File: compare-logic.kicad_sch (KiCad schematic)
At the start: 0 parts

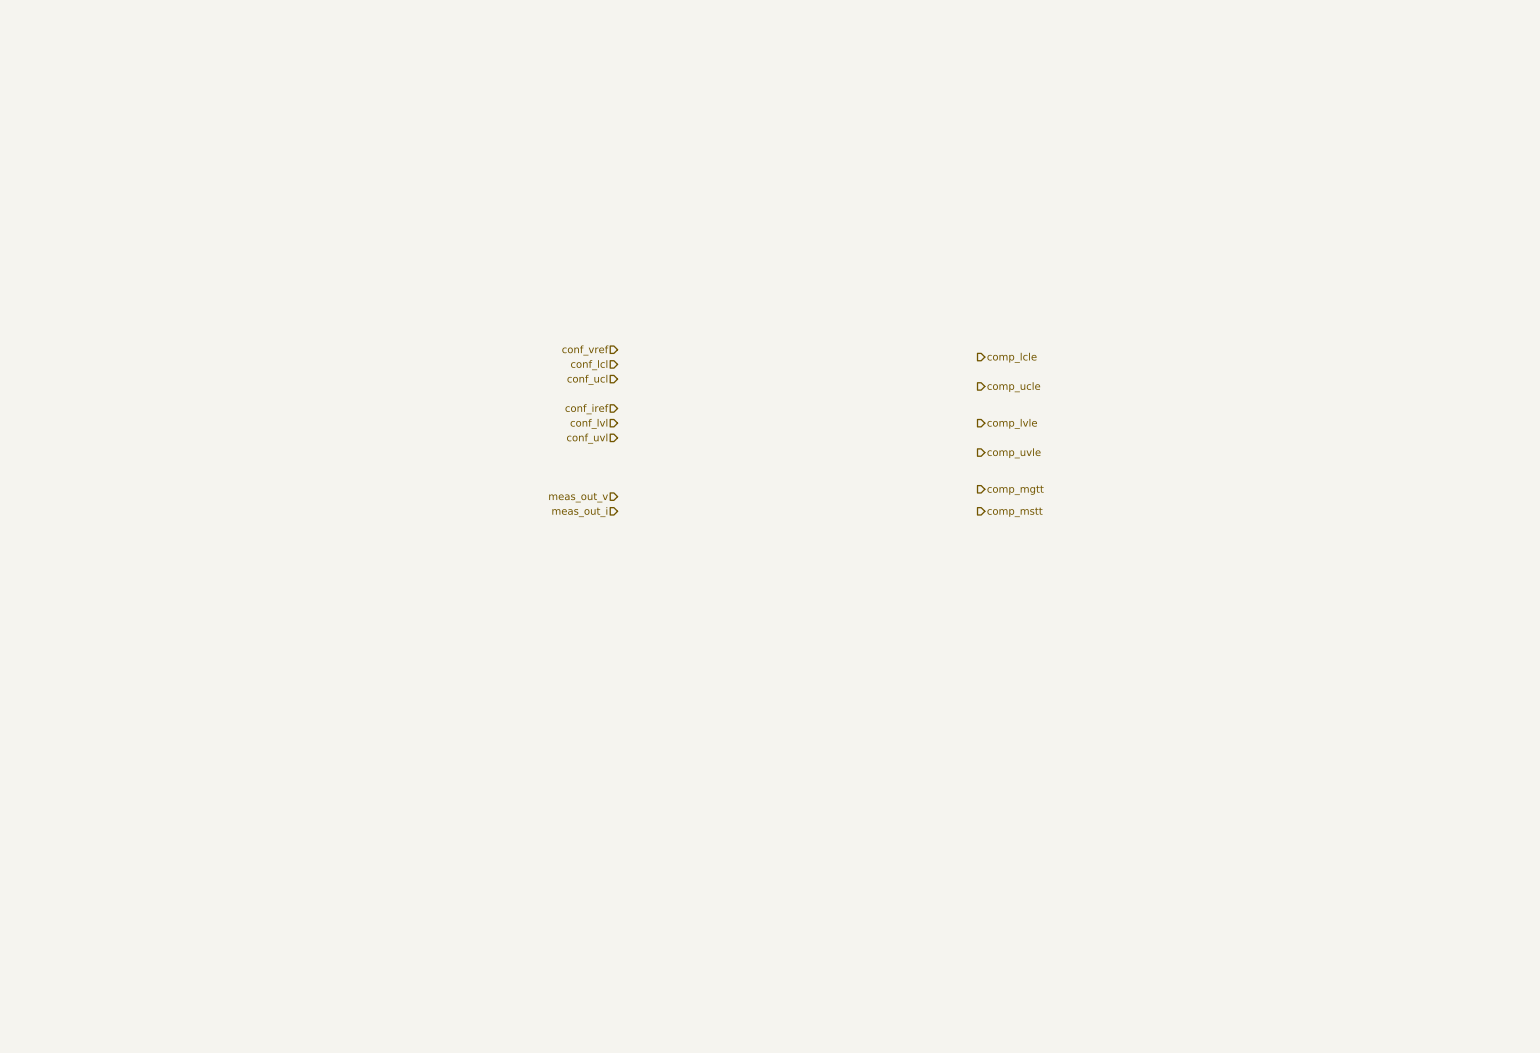
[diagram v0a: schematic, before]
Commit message: add limit-logic comparator opamp tlv9352
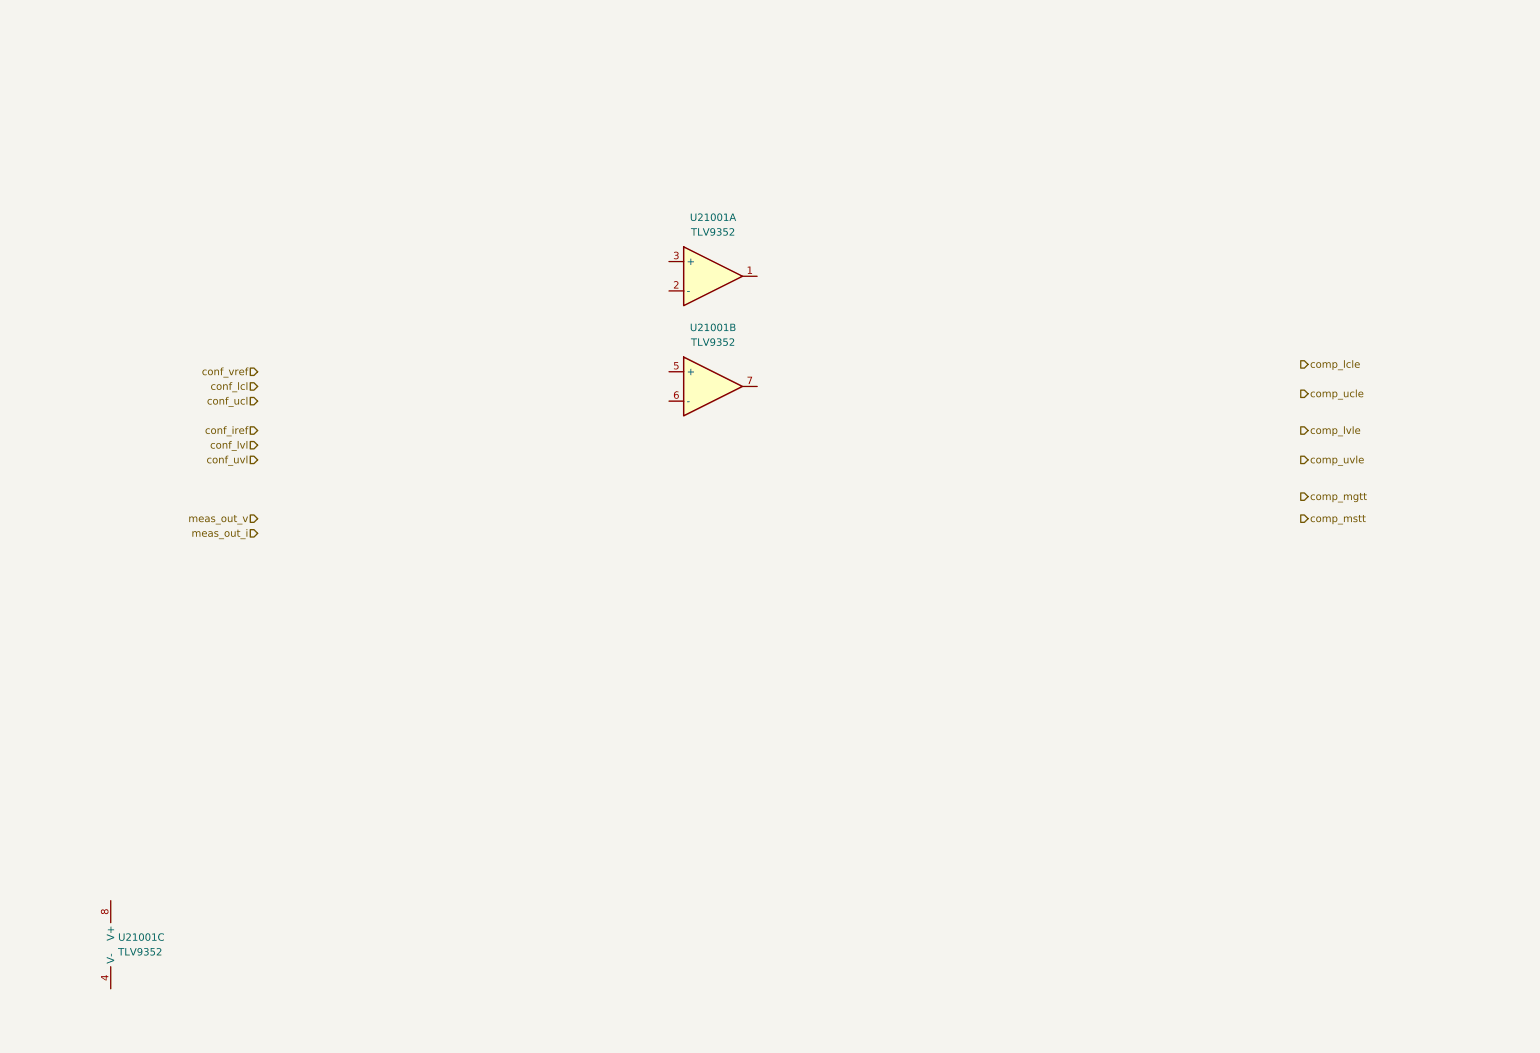
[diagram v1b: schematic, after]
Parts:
- added U21001: TLV9352, Package_SO:SOIC-8_3.9x4.9mm_P1.27mm, symbol pss:Opamp_Dual

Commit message: add compare-logic windows comparator
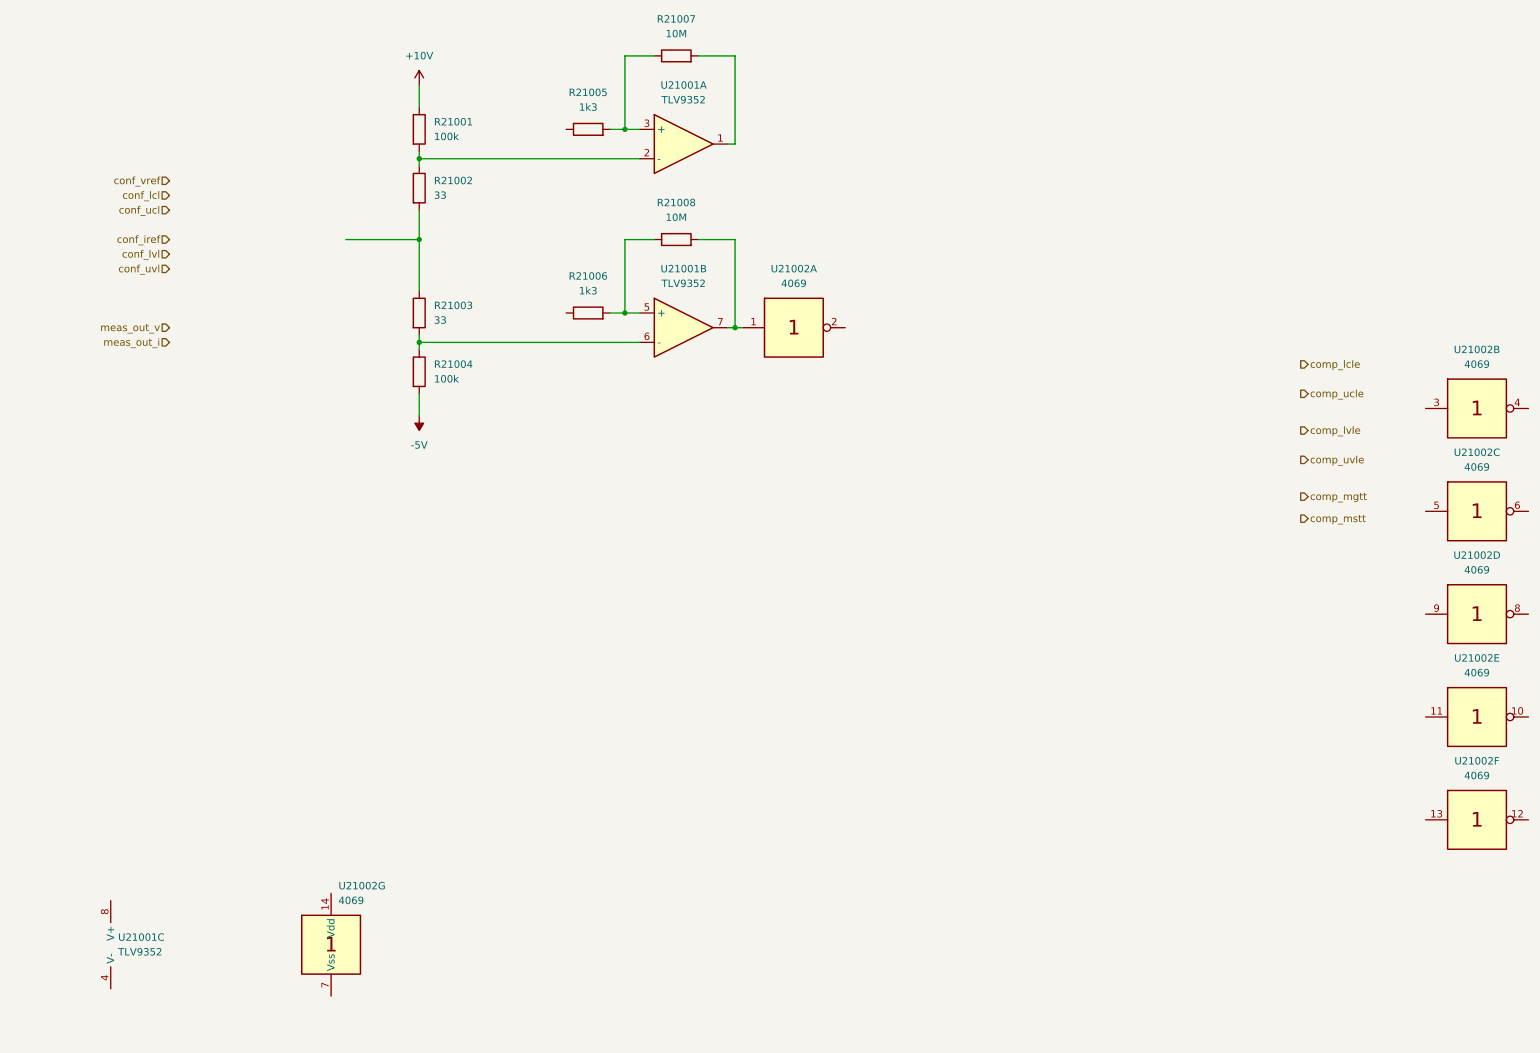
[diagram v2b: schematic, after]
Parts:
- added R21001, R21004: 100k, Resistor_SMD:R_1210_3225Metric_Pad1.30x2.65mm_HandSolder, symbol pss:R
- added R21002, R21003: 33, Resistor_SMD:R_1210_3225Metric_Pad1.30x2.65mm_HandSolder, symbol pss:R
- added R21005, R21006: 1k3, Resistor_SMD:R_1210_3225Metric_Pad1.30x2.65mm_HandSolder, symbol pss:R
- added R21007, R21008: 10M, Resistor_SMD:R_1210_3225Metric_Pad1.30x2.65mm_HandSolder, symbol pss:R
- added U21002: 4069, Package_SO:SOIC-14_3.9x8.7mm_P1.27mm, symbol pss:4069
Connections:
- net at U21001.5 (+): now also R21006.2, R21008.1
- net at U21001.6 (-): now also R21003.2, R21004.1
- net at U21001.7: now also R21008.2, U21002.1
- net at U21001.1: now also R21007.2
- net at U21001.2 (-): now also R21001.2, R21002.1
- net at U21001.3 (+): now also R21005.2, R21007.1
- new net: R21002.2, R21003.1
- new net +10V: R21001.1
- new net -5V: R21004.2
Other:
- moved on the sheet: U21001A, U21001B

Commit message: add window-comparator hirarchical sheet
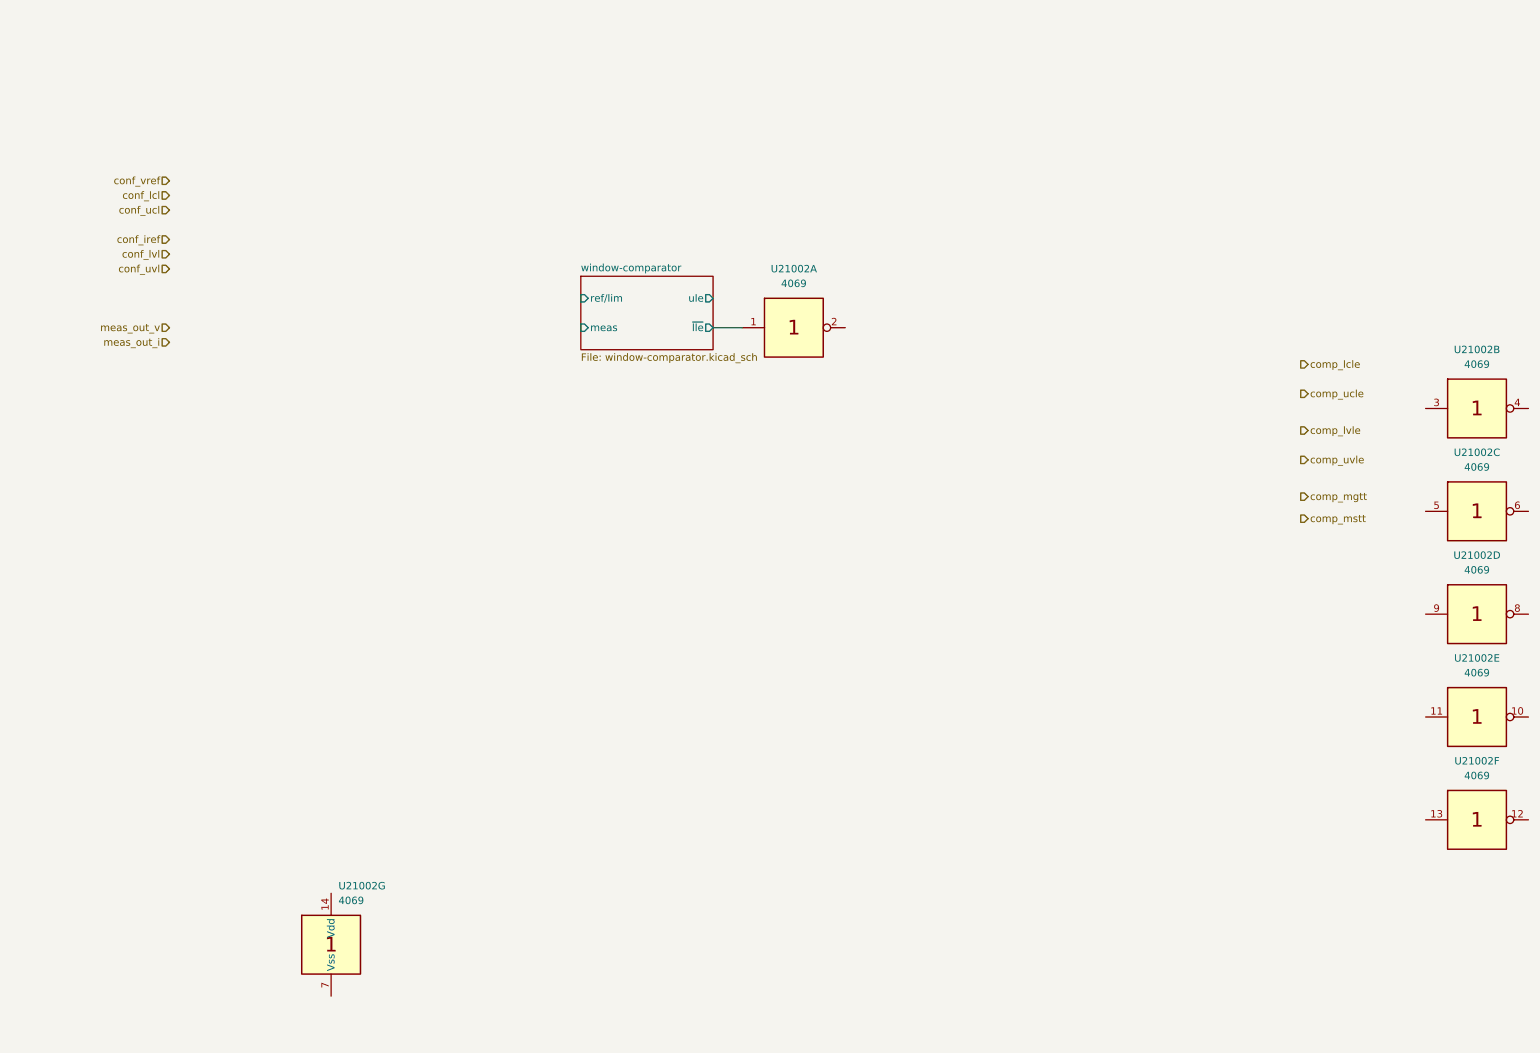
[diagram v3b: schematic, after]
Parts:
- removed R21001, R21004: 100k, Resistor_SMD:R_1210_3225Metric_Pad1.30x2.65mm_HandSolder, symbol pss:R
- removed R21002, R21003: 33, Resistor_SMD:R_1210_3225Metric_Pad1.30x2.65mm_HandSolder, symbol pss:R
- removed R21005, R21006: 1k3, Resistor_SMD:R_1210_3225Metric_Pad1.30x2.65mm_HandSolder, symbol pss:R
- removed R21007, R21008: 10M, Resistor_SMD:R_1210_3225Metric_Pad1.30x2.65mm_HandSolder, symbol pss:R
- removed U21001: TLV9352, Package_SO:SOIC-8_3.9x4.9mm_P1.27mm, symbol pss:Opamp_Dual
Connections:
- net window-comparator/~{lle}: now reaches U21002.1
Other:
- added sheet window-comparator (window-comparator.kicad_sch)

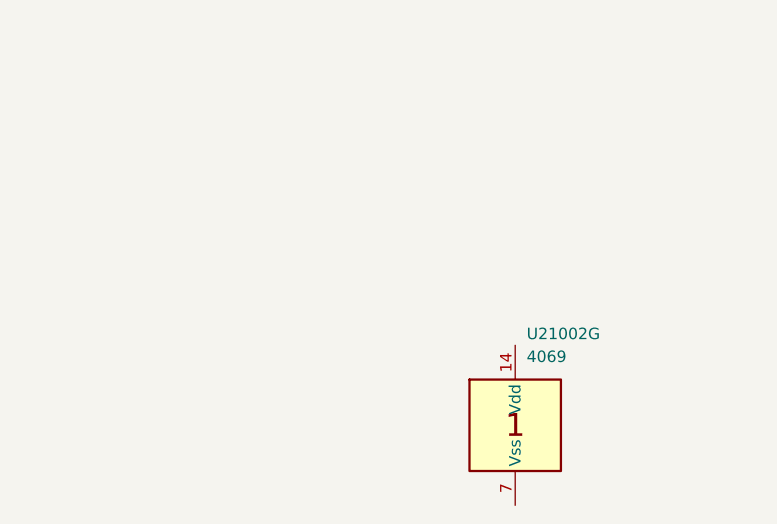
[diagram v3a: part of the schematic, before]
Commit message: add compare-logic decoupling capacitor
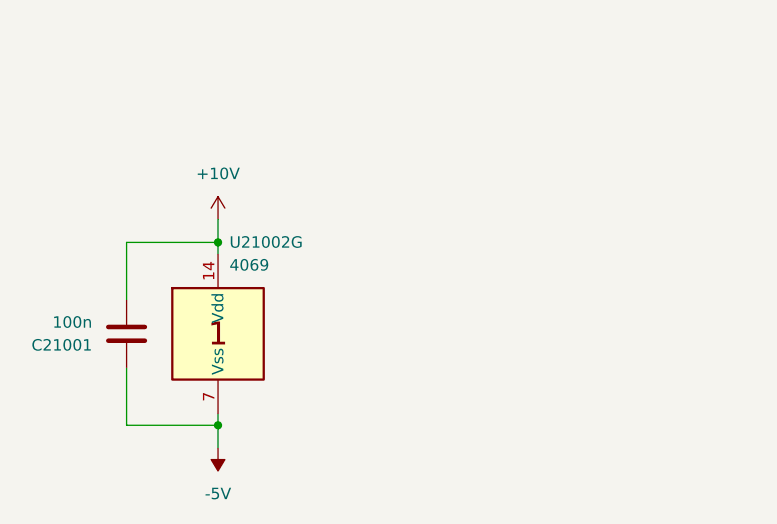
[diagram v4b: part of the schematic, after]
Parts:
- added C21001: 100n, Capacitor_SMD:C_0805_2012Metric_Pad1.18x1.45mm_HandSolder, symbol pss:C
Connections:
- net +10V: now reaches U21002.14 (Vdd)
- net +10V: now also C21001.2
- net -5V: now reaches U21002.7 (Vss)
- net -5V: now also C21001.1
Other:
- moved on the sheet: U21002G

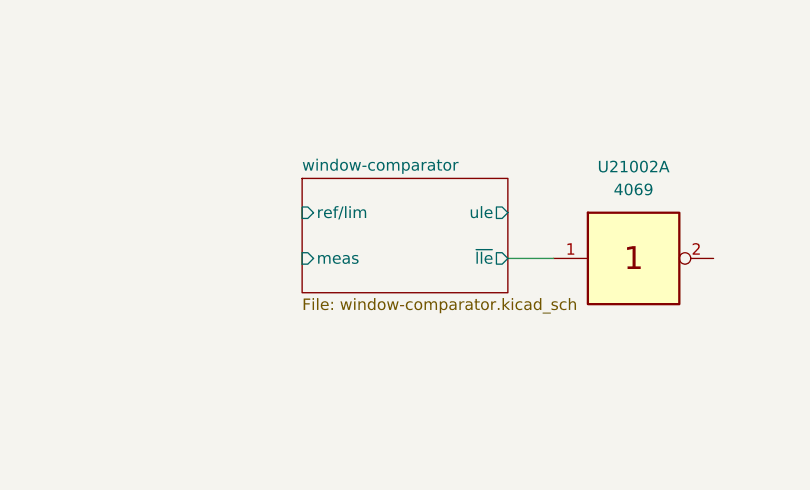
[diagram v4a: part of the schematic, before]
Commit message: fix window-comparator accept two limit inputs
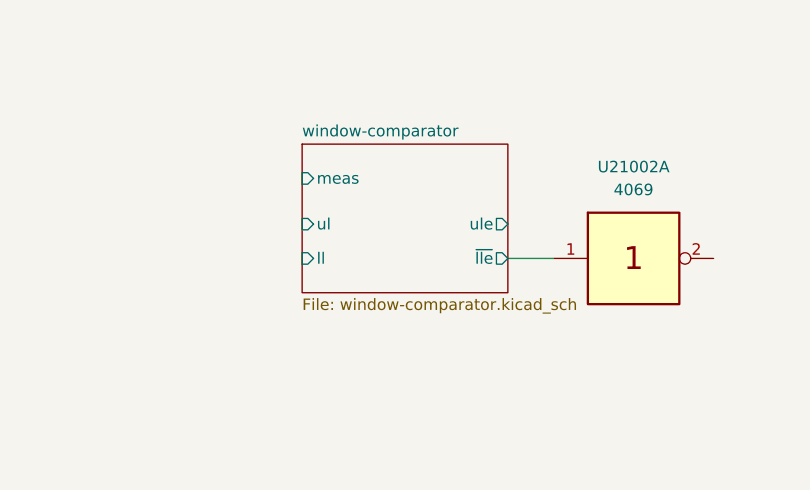
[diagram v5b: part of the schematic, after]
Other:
- sheet window-comparator ports: added ll, ul; removed ref/lim
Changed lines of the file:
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@@
 	)
 	(sheet
-		(at 116.84 63.5)
-		(size 22.86 12.7)
+		(at 116.84 59.69)
+		(size 22.86 16.51)
 		(fields_autoplaced yes)
 		(stroke
@@
 		)
 		(property "Sheetname" "window-comparator"
-			(at 116.84 62.7884 0)
+			(at 116.84 58.9784 0)
 			(effects
 				(font
@@
 		)
 		(pin "ule" output
-			(at 139.7 67.31 0)
+			(at 139.7 68.58 0)
 			(effects
 				(font
@@
 		)
 		(pin "meas" input
+			(at 116.84 63.5 180)
+			(effects
+				(font
+					(size 1.27 1.27)
+				)
+				(justify left)
+			)
+		)
+		(pin "ll" input
 			(at 116.84 72.39 180)
 			(effects
@@
 			)
 		)
-		(pin "ref{slash}lim" input
-			(at 116.84 67.31 180)
+		(pin "ul" input
+			(at 116.84 68.58 180)
 			(effects
 				(font
